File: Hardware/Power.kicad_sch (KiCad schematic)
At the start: 7 parts, among them U2 AP7361C-3.3V

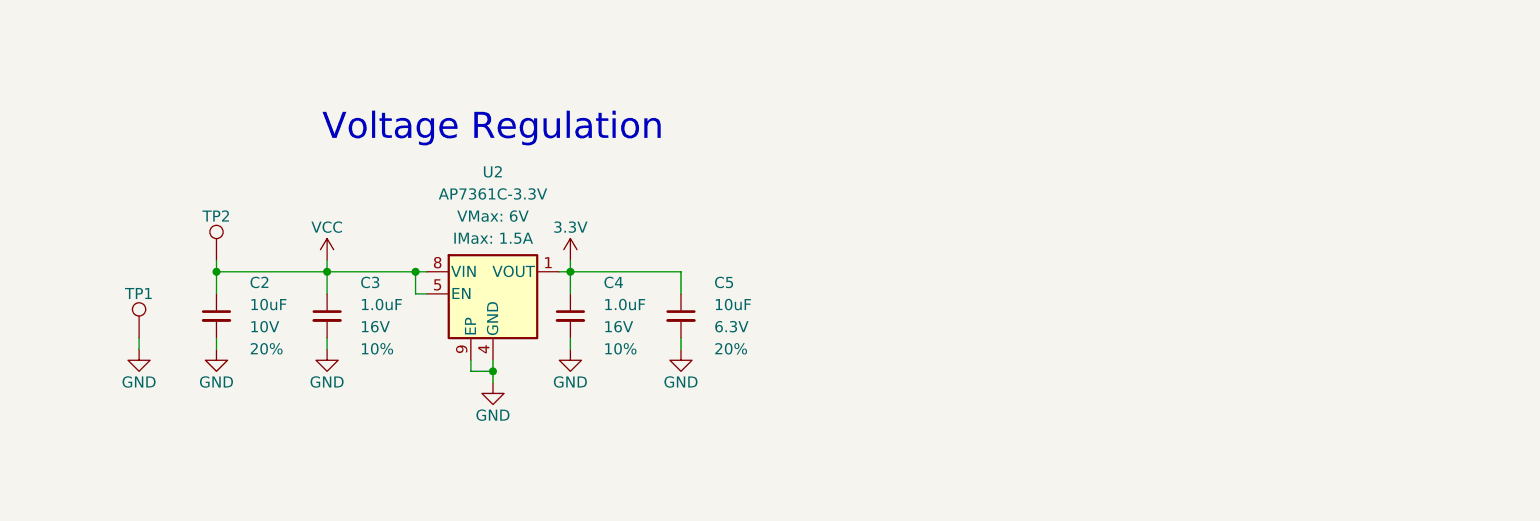
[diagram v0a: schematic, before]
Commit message: Ready for airwire review
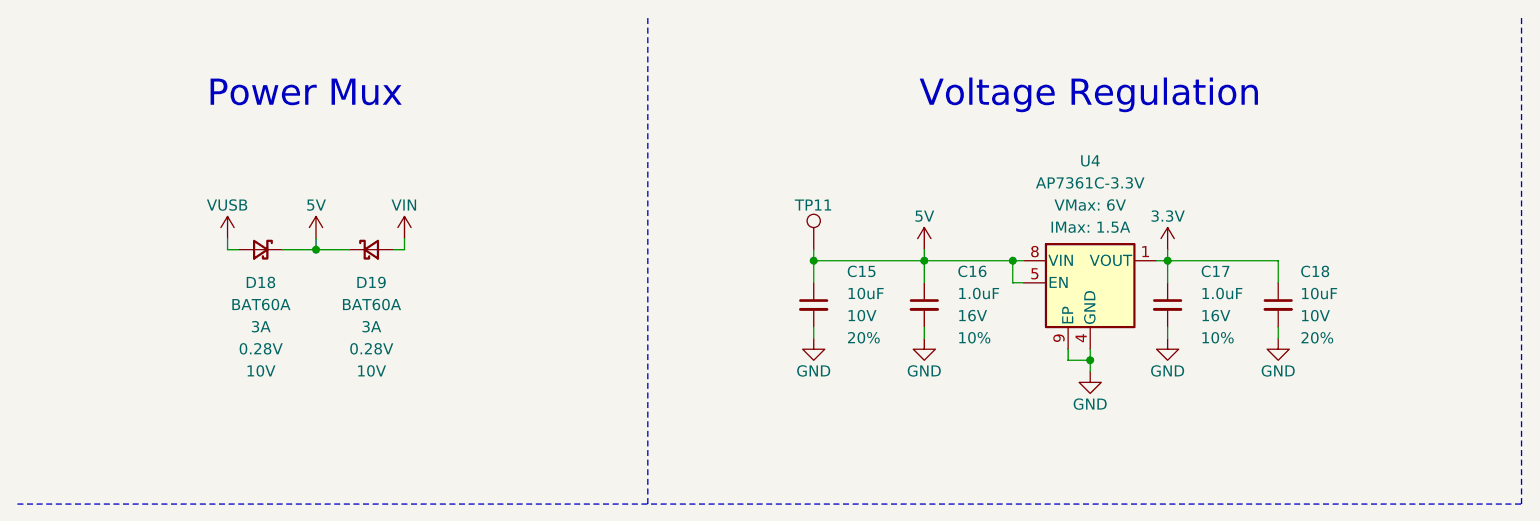
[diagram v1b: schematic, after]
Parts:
- removed C4: 1.0uF, SparkFun-Capacitor:C_0402_1005Metric, symbol SparkFun-Capacitor:1.0uF_0402_16V_10%
- removed C5: 10uF, SparkFun-Capacitor:C_0603_1608Metric, symbol SparkFun-Capacitor:10uF_0603_6.3V_20%
- removed TP1: 1.25mm, SparkFun-Connector:TestPoint-1.25mm, symbol SparkFun-Connector:TestPoint_1.25mm
- added C17: 1.0uF, SparkFun-Capacitor:C_0603_1608Metric, symbol SparkFun-Capacitor:1.0uF_0603_16V_10%
- added C18: 10uF, SparkFun-Capacitor:C_0603_1608Metric, symbol SparkFun-Capacitor:10uF_0603_10V_20%
- added D18, D19: BAT60A, SparkFun-Semiconductor-Standard:SOD-323, symbol SparkFun-DiscreteSemi:D_Schottky_3A_10V_0.28V
- renumbered C2 to C15, C3 to C16, TP2 to TP11, U2 to U4
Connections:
- net 3.3V: now also C17.1, C18.1
- net GND: now also C17.2, C18.2
- net VCC renamed 5V
- net 5V: now also D18.1 (K), D19.1 (K)
- new net VIN: D19.2 (A)
- new net VUSB: D18.2 (A)
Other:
- note added: "Power Mux"
- moved on the sheet: C15, C16, TP11, U4

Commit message: Routed
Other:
- note added: "Voltage Regulation - AP7361C-3.3V"
- note removed: "Voltage Regulation"
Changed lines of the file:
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@@
 		)
 	)
-	(text "Voltage Regulation"
+	(text "Voltage Regulation - AP7361C-3.3V"
 		(exclude_from_sim no)
 		(at 135.89 21.59 0)

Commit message: Schematic updates after proto review
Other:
- title: Power -> SparkFun GNSS mosaic-T - Power
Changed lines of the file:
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@@
 	(paper "USLetter")
 	(title_block
-		(title "Power")
+		(title "SparkFun GNSS mosaic-T - Power")
 	)
 	(text "Power Mux"
